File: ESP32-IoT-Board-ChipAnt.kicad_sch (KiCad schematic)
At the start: 46 parts, among them IC1 ESP32-C3FH4, IC2 CP2102N-A02-GQFN28, J1 USB_B_Micro, J2 Conn_01x05, Q1 Q_NPN_BEC, Q2 Q_NPN_BEC, U1 AMS1117-3.3, U2 USBLC6-2SC6, U3 MCP9700AT-ETT, Y1 40 Mhz Crystal

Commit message: --
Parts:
- removed C15: 10uF, Capacitor_SMD:C_0603_1608Metric, symbol Device:C_Small
- removed IC2: CP2102N-A02-GQFN28, CP2102N-A02-GQFN28:QFN50P500X500X80-29N-D, symbol CP2102N-A02-GQFN28:CP2102N-A02-GQFN28
- removed Q1, Q2: Q_NPN_BEC, Package_TO_SOT_SMD:SOT-23, symbol Device:Q_NPN_BEC
- removed R3, R4: 10k, Resistor_SMD:R_0402_1005Metric, symbol Device:R_Small
- removed R7: 10k(NC), Resistor_SMD:R_0402_1005Metric, symbol Device:R_Small
- removed R8: 1k, Resistor_SMD:R_0402_1005Metric, symbol Device:R_Small
- added J3: Conn_01x05, Connector_PinHeader_2.54mm:PinHeader_1x05_P2.54mm_Vertical, symbol Connector_Generic:Conn_01x05
- added R5: 1k, Resistor_SMD:R_0402_1005Metric, symbol Device:R_Small
- J2: footprint Connector_Molex:Molex_KK-254_AE-6410-05A_1x05_P2.54mm_Vertical -> Connector_PinHeader_2.54mm:PinHeader_1x05_P2.54mm_Vertical
- renumbered C16 to C15, C17 to C16, R5 to R3, R6 to R4, R9 to R6
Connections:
- net +3V3: now also C4.1, U3.1 (Vdd), J3.4 (Pin_4)
- net GND: now also J3.5 (Pin_5), R5.2
- net GPIO9: now also R5.1
- net RXD0: now also J3.3 (Pin_3)
- net TXD0: now also J3.2 (Pin_2)
- net USBLC_D+: now also IC1.26 (GPIO19)
- net USBLC_D-: now also IC1.25 (GPIO18)
- net VBUS: now also J3.1 (Pin_1)
- no-connect marks 33 -> 15
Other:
- note added: "ESP32 C3FH4"
- note added: "Note: To program the ESP32 through UART with a USB-TO-UART converter."
- note added: "USB-TO-UART connector"
- note removed: "Auto Program Circuit"
- note removed: "Auto program"
- note removed: "Currently chosen: Flash using UART Flash using UART: Flash firmware, no debug (only monitor log output) Flash using JTAG: Uses JTAG adapter and OpenOCD to flash and debug the firmware"
- note removed: "DTR RTS—>EN IO9 1 1 1 1 0 0 1 1 1 0 0 1 0 1 1 0"
- note removed: "ESP32 C3 MINI"
- note removed: "Note: Serial-UART Bridge (CP2102N) to program the ESP32 through USB"
- note removed: "USB-UART Bridge"

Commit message: Changed almost everything
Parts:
- removed ANT1: 2450AD18A7250, 2450AD18A:ANTC3216X60N, symbol 2450AD18A7250:2450AD18A7250
- removed C1, C16, C2, C9: 10uF, Capacitor_SMD:C_0603_1608Metric, symbol Device:C_Small
- removed C10, C11, C14, C15, C3, C4: 0.1uF, Capacitor_SMD:C_0603_1608Metric, symbol Device:C_Small
- removed C12, C13: TBD, Capacitor_SMD:C_0402_1005Metric, symbol Device:C_Small
- removed C5: 1uF, Capacitor_SMD:C_0603_1608Metric, symbol Device:C_Small
- removed C6: 10nF, Capacitor_SMD:C_0603_1608Metric, symbol Device:C_Small
- removed C7, C8: 12pF, Capacitor_SMD:C_0603_1608Metric, symbol Device:C_Small
- removed D1: D_Schottky, Diode_SMD:D_SOD-123, symbol Device:D_Schottky
- removed D2: PWR_LED, LED_SMD:LED_0603_1608Metric, symbol Device:LED
- removed FB1: 600 @ 100Mhz, Inductor_SMD:L_1206_3216Metric, symbol Device:Ferrite_Bead_Small
- removed H1, H2, H3: MountingHole 3mm, MountingHole:MountingHole_3mm_Pad_Via, symbol Mechanical:MountingHole
- removed IC1: ESP32-C3FH4, ESP32-C3FH4:QFN50P500X500X90-33N-D, symbol ESP32-C3FH4:ESP32-C3FH4
- removed J1: USB_B_Micro, Connector_USB:USB_Micro-B_Molex_47346-0001, symbol Connector:USB_B_Micro
- removed J2, J3: Conn_01x05, Connector_PinHeader_2.54mm:PinHeader_1x05_P2.54mm_Vertical, symbol Connector_Generic:Conn_01x05
- removed L1: 2nH, Inductor_SMD:L_0603_1608Metric, symbol Device:L
- removed L2: TBD, Inductor_SMD:L_0402_1005Metric, symbol Device:L
- removed R1: 0R, Resistor_SMD:R_0603_1608Metric, symbol Device:R_Small
- removed R2, R5: 1k, Resistor_SMD:R_0402_1005Metric, symbol Device:R_Small
- removed R3, R4, R6: 10k, Resistor_SMD:R_0402_1005Metric, symbol Device:R_Small
- removed S1: RKB2SJM250SMTR_LFS (Button), RKB2SJM250SMTR LFS:RKB2SJM250SMTRLFS, symbol RKB2SJM250SMTR_LFS:RKB2SJM250SMTR_LFS
- removed U1: AMS1117-3.3, Package_TO_SOT_SMD:SOT-223-3_TabPin2, symbol Regulator_Linear:AMS1117-3.3
- removed U2: USBLC6-2SC6, Package_TO_SOT_SMD:SOT-23-6, symbol Power_Protection:USBLC6-2SC6
- removed U3: MCP9700AT-ETT, Package_TO_SOT_SMD:SOT-23, symbol Sensor_Temperature:MCP9700AT-ETT
- removed Y1: 40 Mhz Crystal, ECS-400-10-37B:ECS4001037B2CKMTR, symbol Device:Crystal_GND24
- added TP1: RX, TestPoint:TestPoint_Pad_D1.0mm, symbol Connector:TestPoint
- added TP2: TX, TestPoint:TestPoint_Pad_D1.0mm, symbol Connector:TestPoint
- added TP3: +3V3, TestPoint:TestPoint_Pad_D1.0mm, symbol Connector:TestPoint
- added TP4: GND, TestPoint:TestPoint_Pad_D1.0mm, symbol Connector:TestPoint
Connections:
- net +3V3: now also TP3.1
- net GND: now also TP4.1
- net RXD0: now also TP1.1
- net TXD0: now also TP2.1
- no-connect marks 15 -> 0
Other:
- added sheet MCU, Crystal & Antenna. (MCU.kicad_sch)
- added sheet Sensors (Sensors.kicad_sch)
- added sheet USB & Power (untitled.kicad_sch)
- note added: "USB-TO-UART connector (old)"
- note removed: "CL = (C1 * C2)/(C1 + C2) + C_stray C_stray in a 3.3VDC circuit is often 3~4pF CL = 10 pF (datasheet) CL = (12 * 12)/(12 + 12) + 4 = 10 C1 = C2 = 12 pF"
- note removed: "Crystal"
- note removed: "ESP32 C3FH4"
- note removed: "INMP441 (MEMS I2S Microphone) connector"
- note removed: "MCP9700 (Linear Thermistor)"
- note removed: "Resistor footprint to measure current total consumption."
- note removed: "Strapping pins (Booting mode)"
- note removed: "USB & Power Supply"
- note removed: "USB-TO-UART connector"
- note removed: "VDD_SPI floating? ok?"

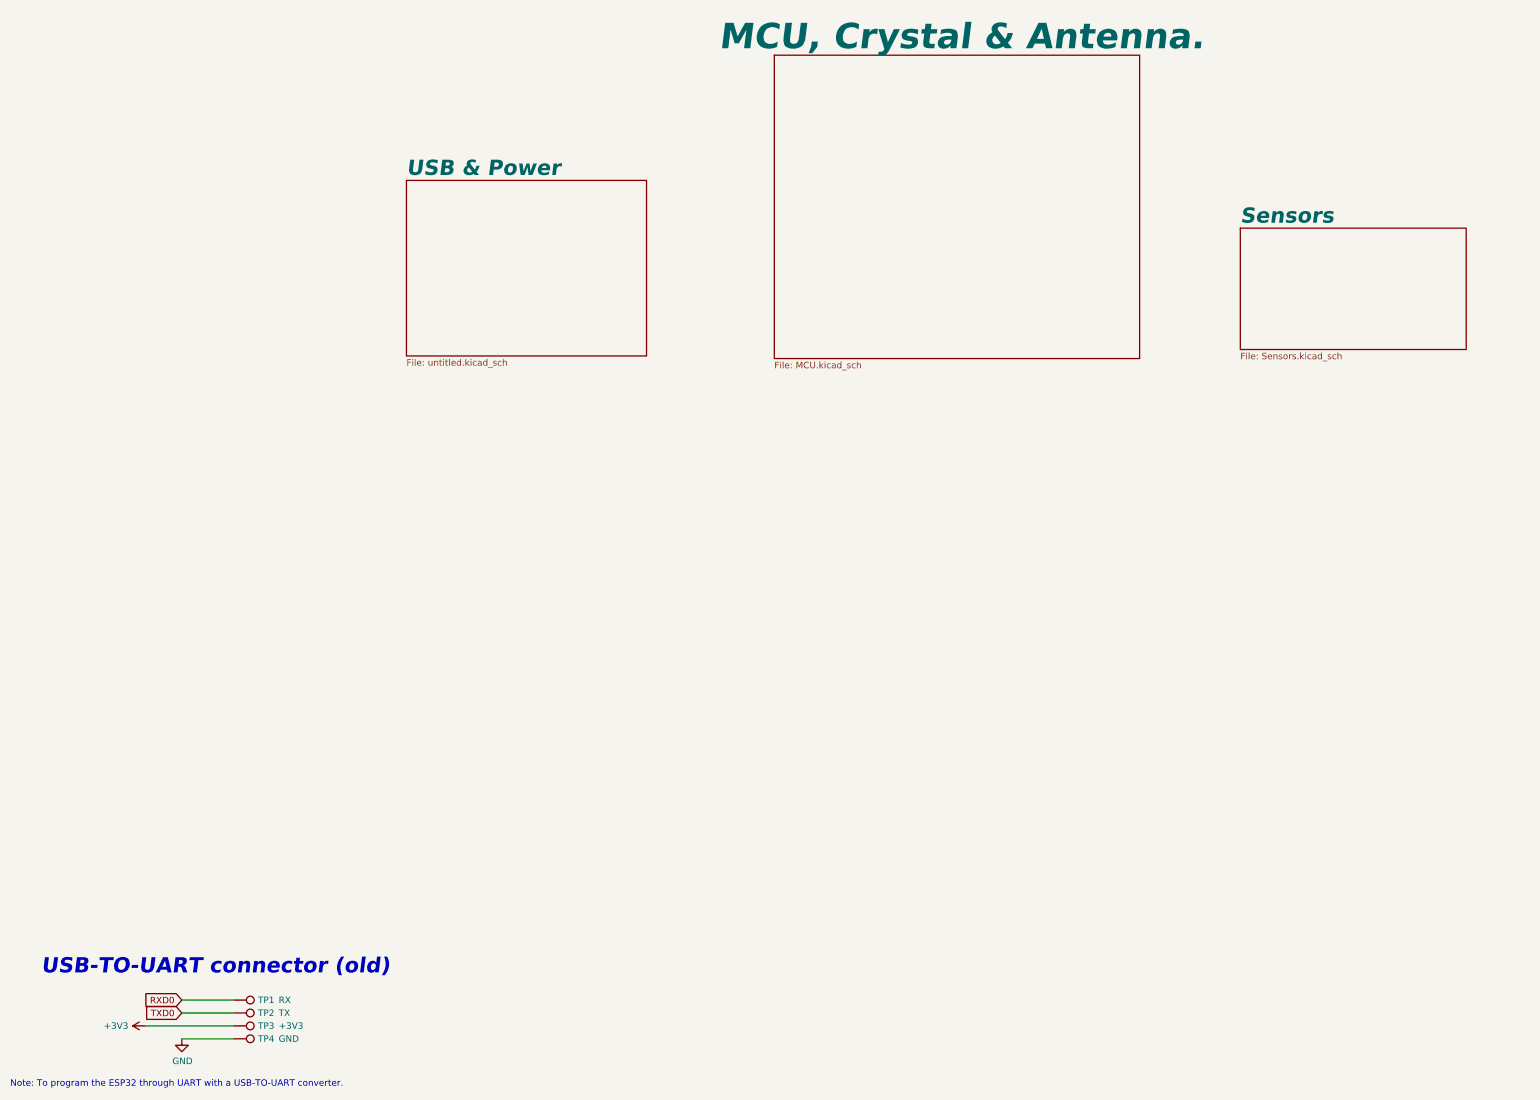
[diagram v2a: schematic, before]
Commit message: Added accelerometer
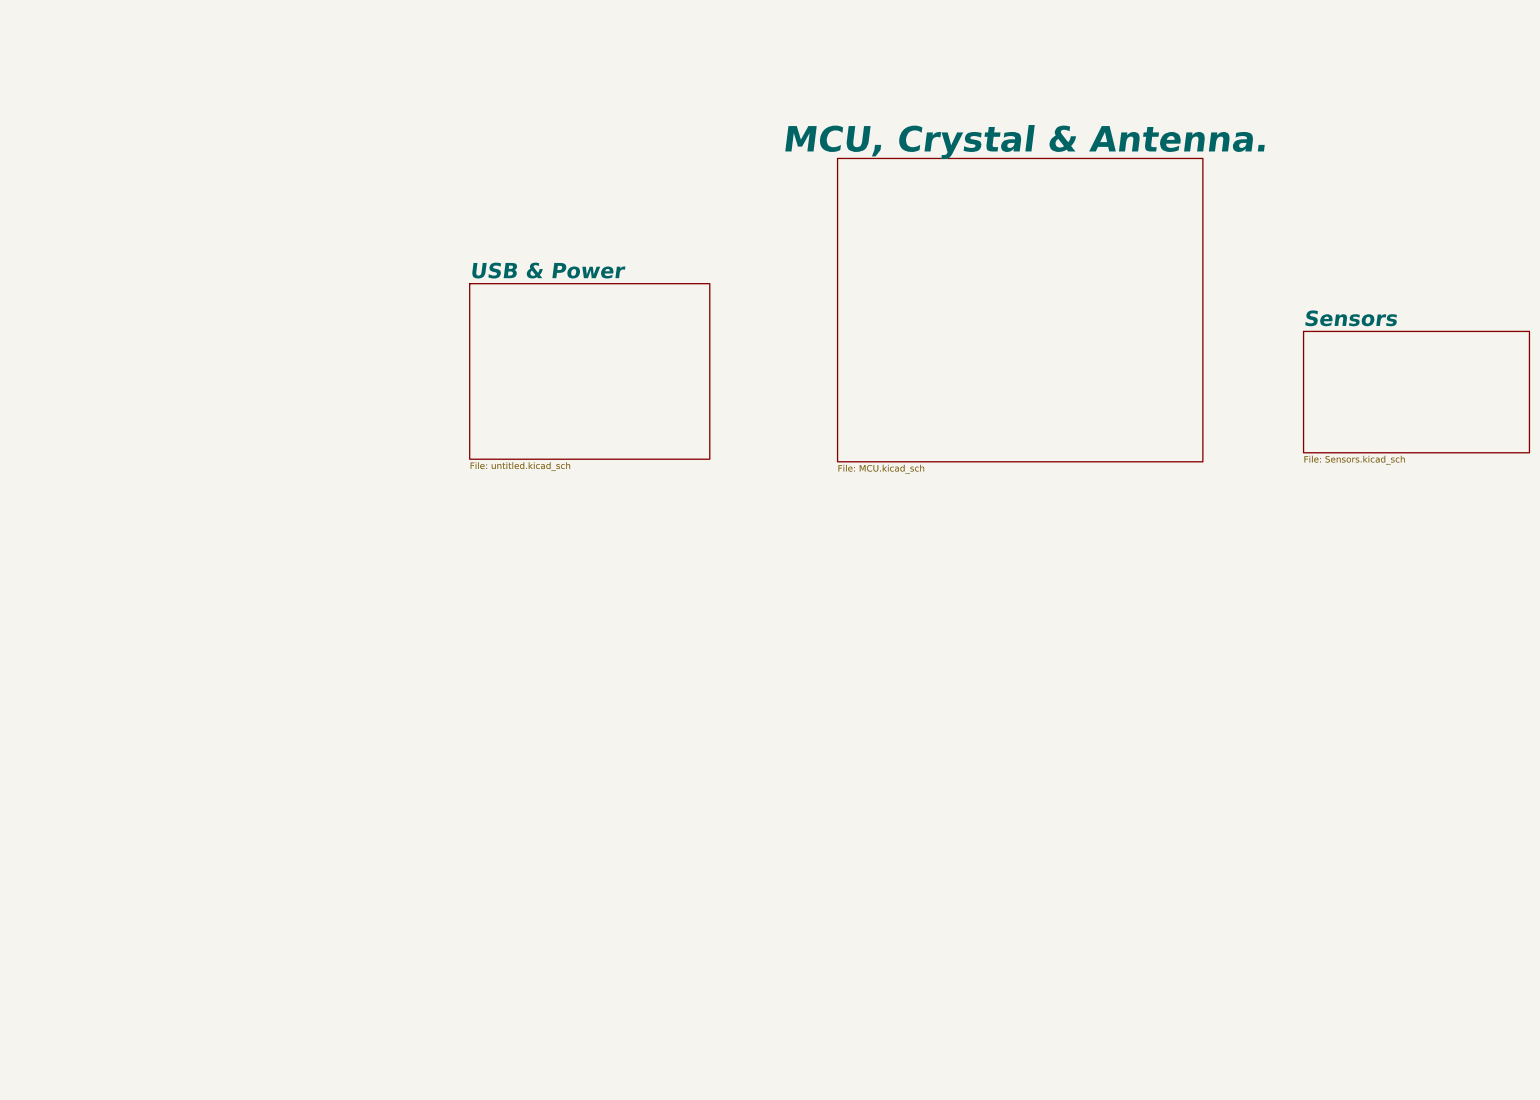
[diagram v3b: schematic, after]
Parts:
- removed TP1: RX, TestPoint:TestPoint_Pad_D1.0mm, symbol Connector:TestPoint
- removed TP2: TX, TestPoint:TestPoint_Pad_D1.0mm, symbol Connector:TestPoint
- removed TP3: +3V3, TestPoint:TestPoint_Pad_D1.0mm, symbol Connector:TestPoint
- removed TP4: GND, TestPoint:TestPoint_Pad_D1.0mm, symbol Connector:TestPoint
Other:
- note removed: "Note: To program the ESP32 through UART with a USB-TO-UART converter."
- note removed: "USB-TO-UART connector (old)"
